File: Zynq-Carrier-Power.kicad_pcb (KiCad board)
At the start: 2 copper layers, 49 x 41 mm, 36 parts, among them J1 Zynq_SoM, J10 Barrel_Jack_MountingPin, J2 B2B-PH-K-S, J3 USB_C_Receptacle_USB2.0_16P, J4 Conn_01x03, J5 Conn_01x03, J6 Conn_01x03, J7 Conn_01x02, J8 Conn_01x02, J9 Conn_01x03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

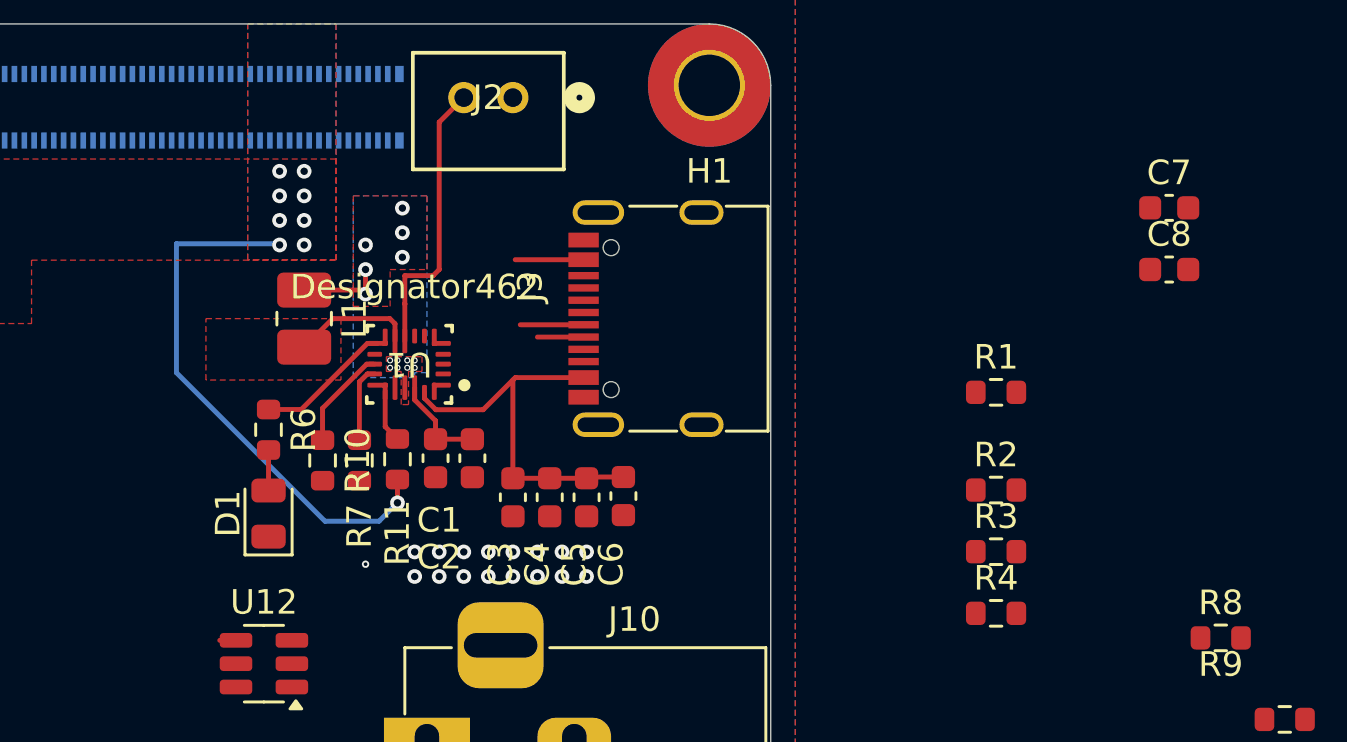
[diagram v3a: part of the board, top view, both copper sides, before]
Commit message: Capacitor Relocation
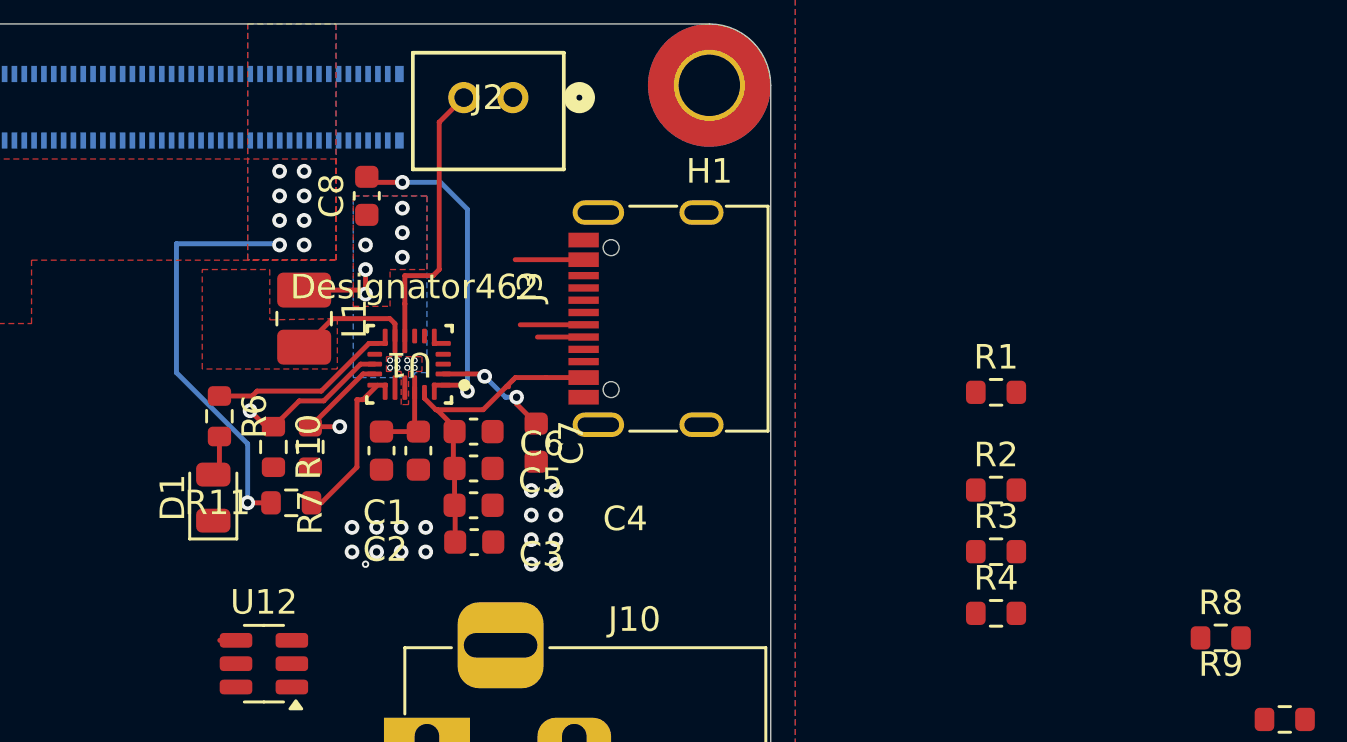
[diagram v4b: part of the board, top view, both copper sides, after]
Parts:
- moved C8 32.8 mm to (129.8, 107.6), turned to 90 degrees
- moved C7 27.5 mm to (136.7, 117.7), turned to -90 degrees
- moved C6 6.64 mm to (134.1, 117.2), turned to 0 degrees
- moved C5 4.75 mm to (134.1, 118.7), turned to 0 degrees
- moved R11 4.68 mm to (126.7, 120.1), turned to 180 degrees
- moved C4 3.12 mm to (134.1, 120.2), turned to 0 degrees
- moved C3 2.41 mm to (134.2, 121.7), turned to 0 degrees
- moved D1 2.34 mm to (123.5, 119.9)
- moved C1 2.22 mm to (130.4, 118.0)
- moved C2 2.22 mm to (131.9, 118.0)
- moved R7 2.07 mm to (127.5, 117.9)
- moved R10 2.07 mm to (126.0, 117.9)
- moved R6 2.07 mm to (123.8, 116.6)
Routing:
- net Net-(U1-BTST): track 0.00 -> 13.3 mm, vias 0 -> 2
- net +5V: track 22.2 -> 16.9 mm
- net Net-(U1-REGN): track 0.00 -> 4.89 mm, vias 0 -> 2
- net /~{CSn}: track 2.15 -> 6.28 mm
- net V_USB: track 18.8 -> 16.1 mm
- net /SDA: track 4.17 -> 6.40 mm, vias 0 -> 1
- net Net-(U1-STAT): track 5.55 -> 7.32 mm
- net /SCL: track 3.13 -> 4.71 mm, vias 0 -> 1
- net Net-(U1-PMID): track 4.21 -> 3.61 mm

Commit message: routed D+D-
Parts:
- removed C5: 10uf, Capacitor_SMD:C_0603_1608Metric
- removed C6: 0.1uf, Capacitor_SMD:C_0603_1608Metric
- R3, U12: moved to B.Cu
- moved J5 29.7 mm to (139.3, 123.4), turned to 90 degrees
- moved J4 28.4 mm to (139.2, 119.9), turned to 90 degrees
- moved U12 21.9 mm to (142.3, 112.6), turned to 0 degrees
- moved R3 14.7 mm to (142.5, 115.1)
- moved C3 3.77 mm to (133.4, 118.0), turned to -90 degrees
- moved C4 2.34 mm to (134.9, 118.0), turned to -90 degrees
- moved C7 2.26 mm to (135.5, 115.7), turned to 0 degrees
- moved R2 1.73 mm to (155.4, 117.9)
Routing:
- net /USB_POW_D+: track 0.00 -> 17.1 mm
- net /USB_D-: track 1.88 -> 17.8 mm, vias 0 -> 1
- net /USB_D+: track 2.58 -> 18.2 mm, vias 0 -> 1
- net /USB_POW_D-: track 0.00 -> 13.1 mm
- net V_USB: track 16.1 -> 6.71 mm, vias 0 -> 3
- net Net-(U12-VP): track 0.00 -> 3.41 mm
- net Net-(U1-REGN): track 4.89 -> 2.64 mm, vias 2 -> 0
- net VBAT: vias 0 -> 1
- net GND: vias 17 -> 11
- added copper zone on F.Cu, net V_USB

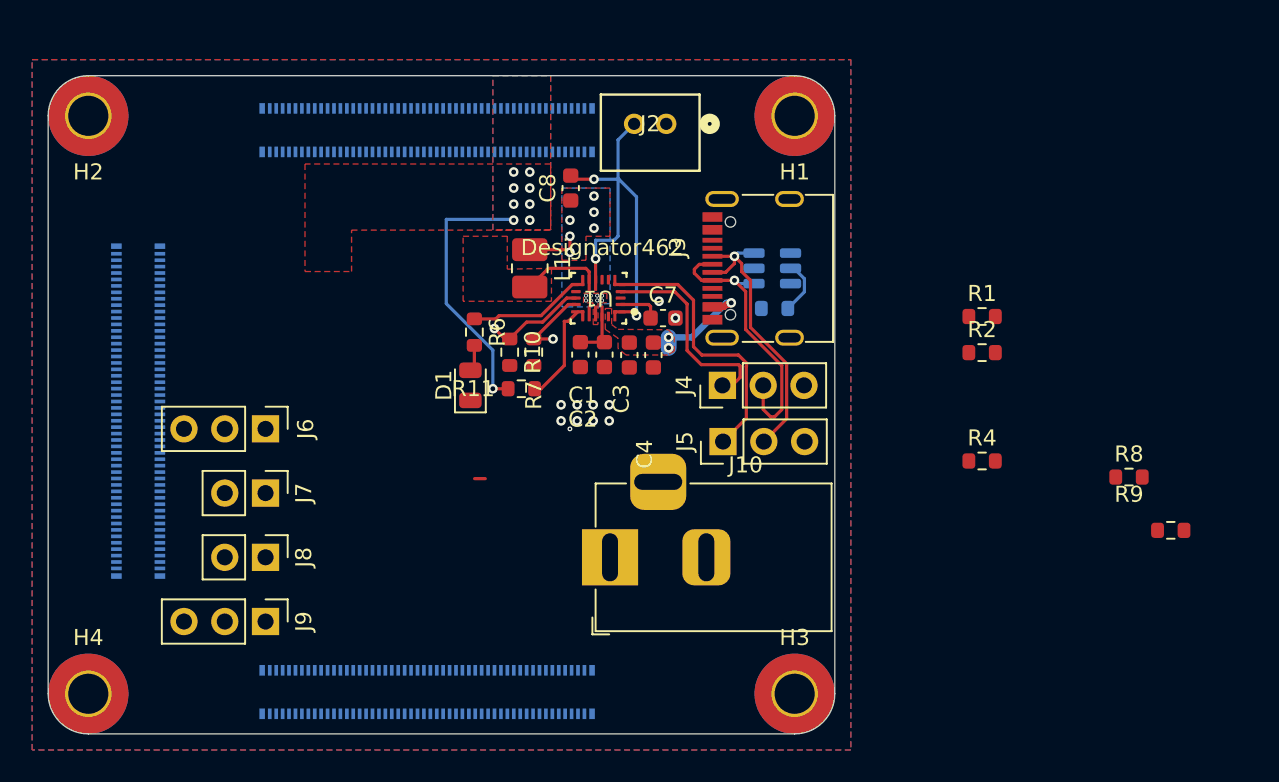
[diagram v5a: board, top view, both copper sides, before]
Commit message: Moved barrel jack & routed a differential pair
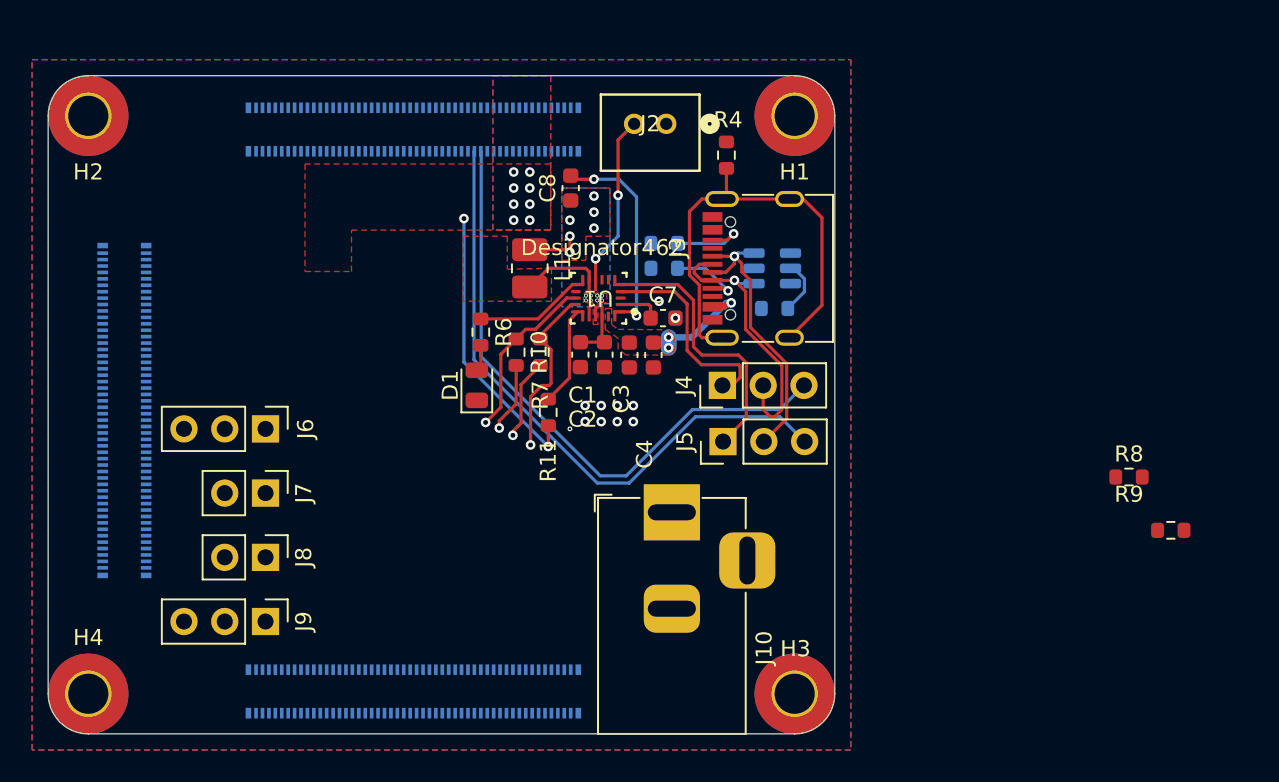
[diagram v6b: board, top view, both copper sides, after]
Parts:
- R1, R2: moved to B.Cu
- moved R4 24.8 mm to (139.5, 105.6), turned to 90 degrees
- moved R2 20.9 mm to (135.6, 111.1)
- moved R1 20.0 mm to (135.6, 112.6)
- moved J10 4.76 mm to (136.1, 127.8), turned to 90 degrees
- moved R11 2.23 mm to (128.4, 121.6), turned to -90 degrees
- moved J1 0.86 mm to (145.8, 100.5)
- moved D1 0.40 mm to (123.9, 119.9)
- moved R10 0.40 mm to (126.4, 117.9)
- moved R6 0.40 mm to (124.2, 116.6)
- moved R7 0.40 mm to (127.9, 117.9)
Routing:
- net /USB_SOM_D+: track 0.00 -> 39.1 mm
- net /USB_SOM_D-: track 0.00 -> 38.3 mm
- net Net-(J3-SHIELD): track 0.00 -> 28.8 mm
- net /SCL: track 4.71 -> 10.9 mm
- net Net-(J3-CC2): track 0.00 -> 5.23 mm, vias 0 -> 1
- net Net-(J6-Pin_1): track 0.00 -> 5.05 mm, vias 0 -> 1
- net /SDA: track 6.40 -> 11.3 mm
- net Net-(J3-CC1): track 0.00 -> 4.76 mm, vias 0 -> 1
- net Net-(J6-Pin_2): track 0.00 -> 4.33 mm, vias 0 -> 1
- net +5V: track 16.9 -> 17.7 mm, vias 9 -> 10
- net VBAT: track 11.6 -> 10.9 mm, vias 1 -> 2
- net unconnected-(U12-IO3-Pad4): track 0.66 -> 0.00 mm

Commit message: More Connections & DRC
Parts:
- moved R9 38.0 mm to (129.2, 126.1), turned to -90 degrees
- moved R8 37.3 mm to (127.2, 126.1), turned to -90 degrees
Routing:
- net Net-(J8-Pin_1): track 0.00 -> 21.0 mm
- net Net-(J7-Pin_1): track 0.00 -> 16.6 mm
- net GND: track 0.00 -> 16.0 mm, vias 11 -> 12
- net +5V: track 17.7 -> 21.7 mm

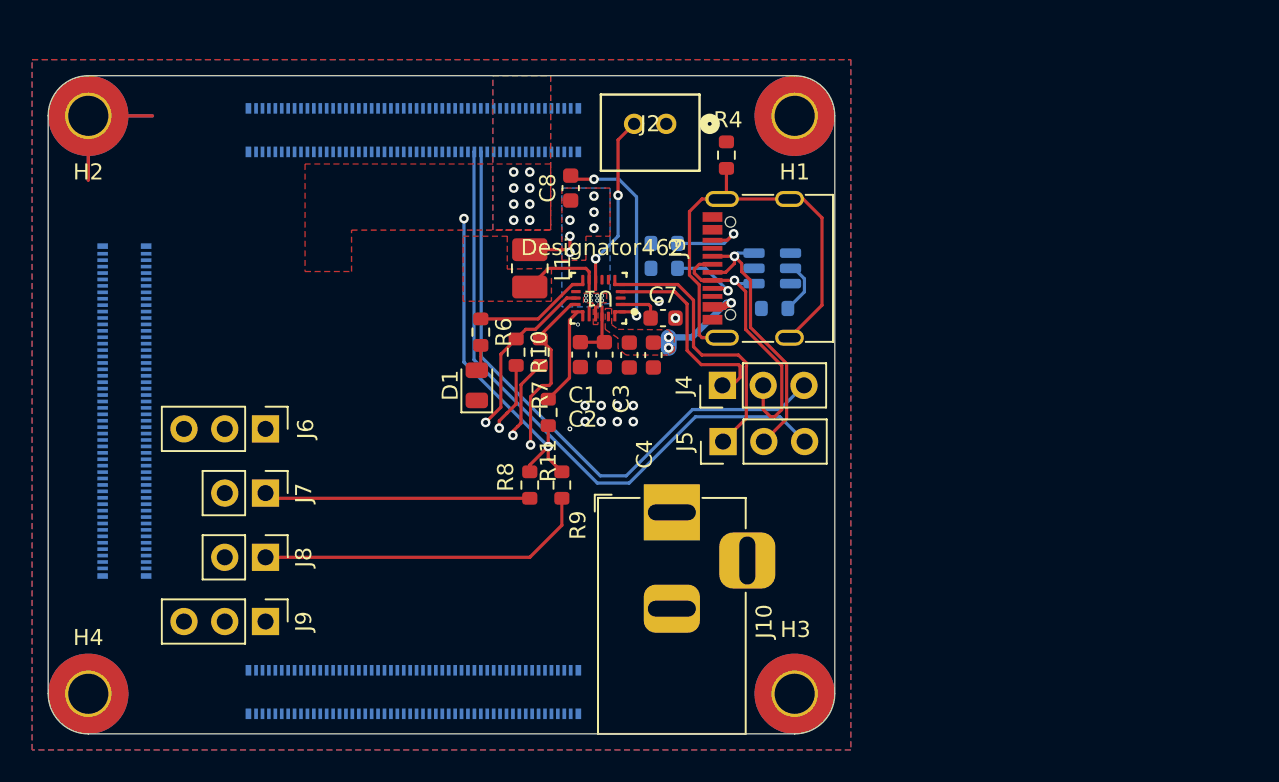
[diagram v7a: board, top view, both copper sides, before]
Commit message: Finished Connections
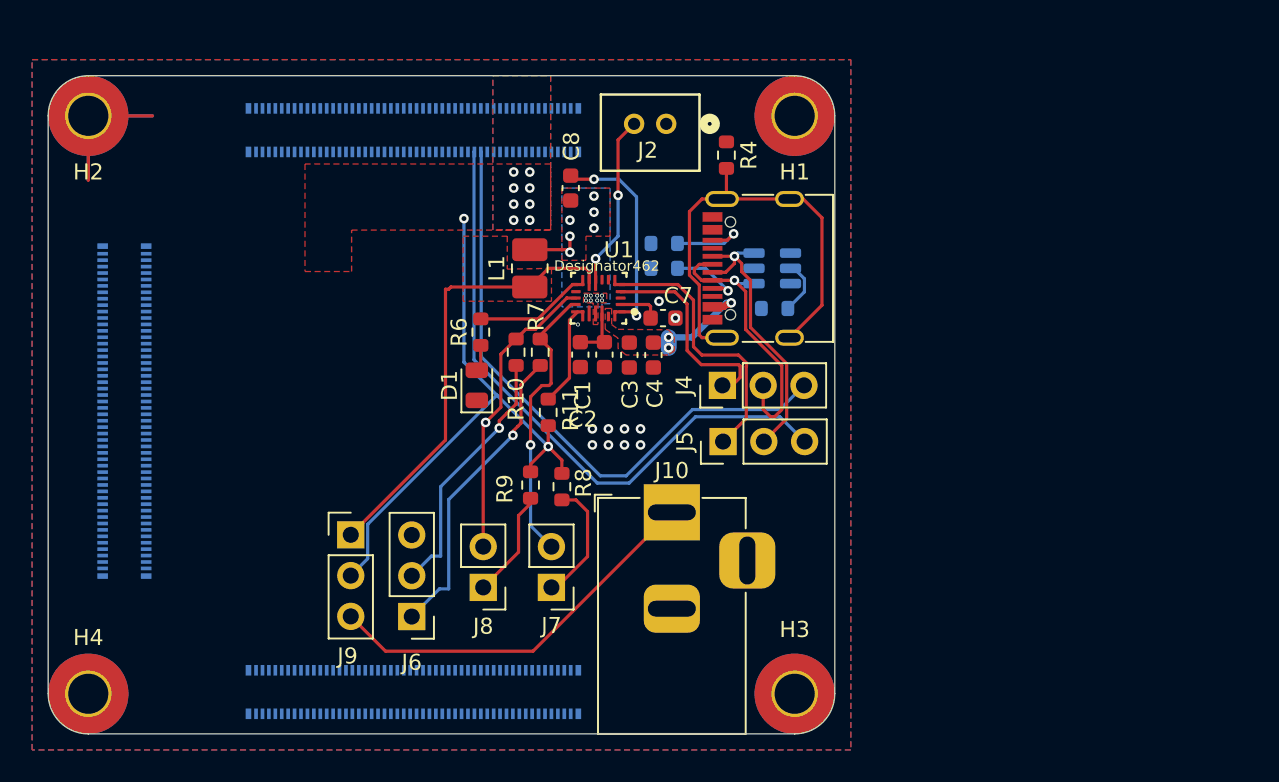
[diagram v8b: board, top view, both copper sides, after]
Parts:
- moved J7 18.8 mm to (128.6, 132.5), turned to 180 degrees
- moved J6 14.8 mm to (119.9, 134.3), turned to 180 degrees
- moved J8 13.7 mm to (124.3, 132.5), turned to 180 degrees
- moved J9 7.57 mm to (116.1, 129.2), turned to 0 degrees
- moved R8 2.00 mm to (129.2, 126.2)
- moved R9 1.95 mm to (127.3, 126.1)
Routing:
- net Vps: track 0.00 -> 24.5 mm
- net VREG_OUT: track 4.97 -> 28.0 mm
- net +5V: track 21.7 -> 36.7 mm
- net Net-(J6-Pin_1): track 5.05 -> 19.3 mm
- net Net-(J8-Pin_1): track 21.0 -> 6.77 mm
- net Net-(J6-Pin_2): track 4.33 -> 17.0 mm
- net Net-(J7-Pin_1): track 16.6 -> 7.75 mm
- net /SDA: track 11.3 -> 19.1 mm
- net /SCL: track 10.9 -> 17.8 mm
- net GND: vias 12 -> 11
